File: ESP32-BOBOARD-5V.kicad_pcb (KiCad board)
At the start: 4 copper layers, 100 x 60 mm, 28 parts, among them J1 Conn_01x15, J2 Conn_01x15, J3 Conn_02x16_Counter_Clockwise, J4 Conn_01x03_Male, J5 DX07S016JA1R1500, U1 TXS0108EPW, U3 TXS0108EPW, U4 TXS0108EPW

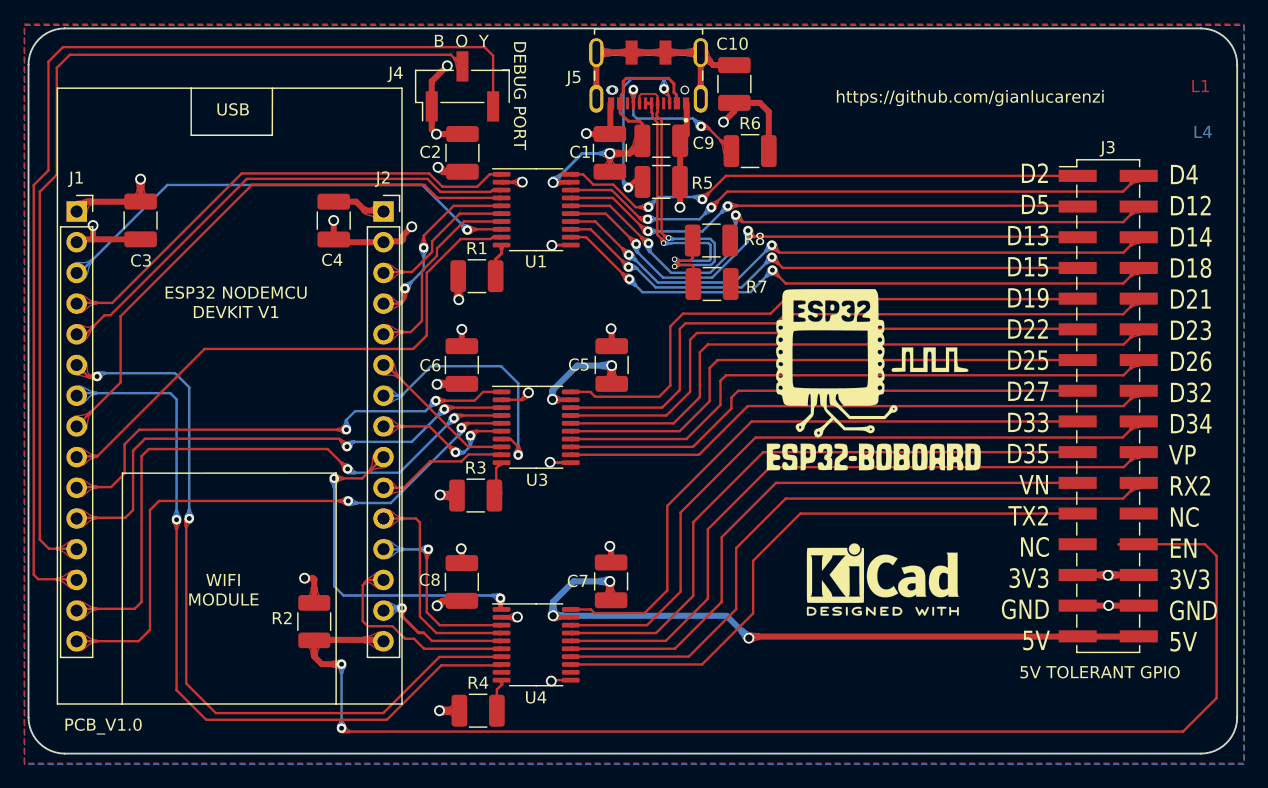
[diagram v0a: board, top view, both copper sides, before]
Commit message: Added the dip-switch for programming Added the ESP32 BOBOARD LOGO
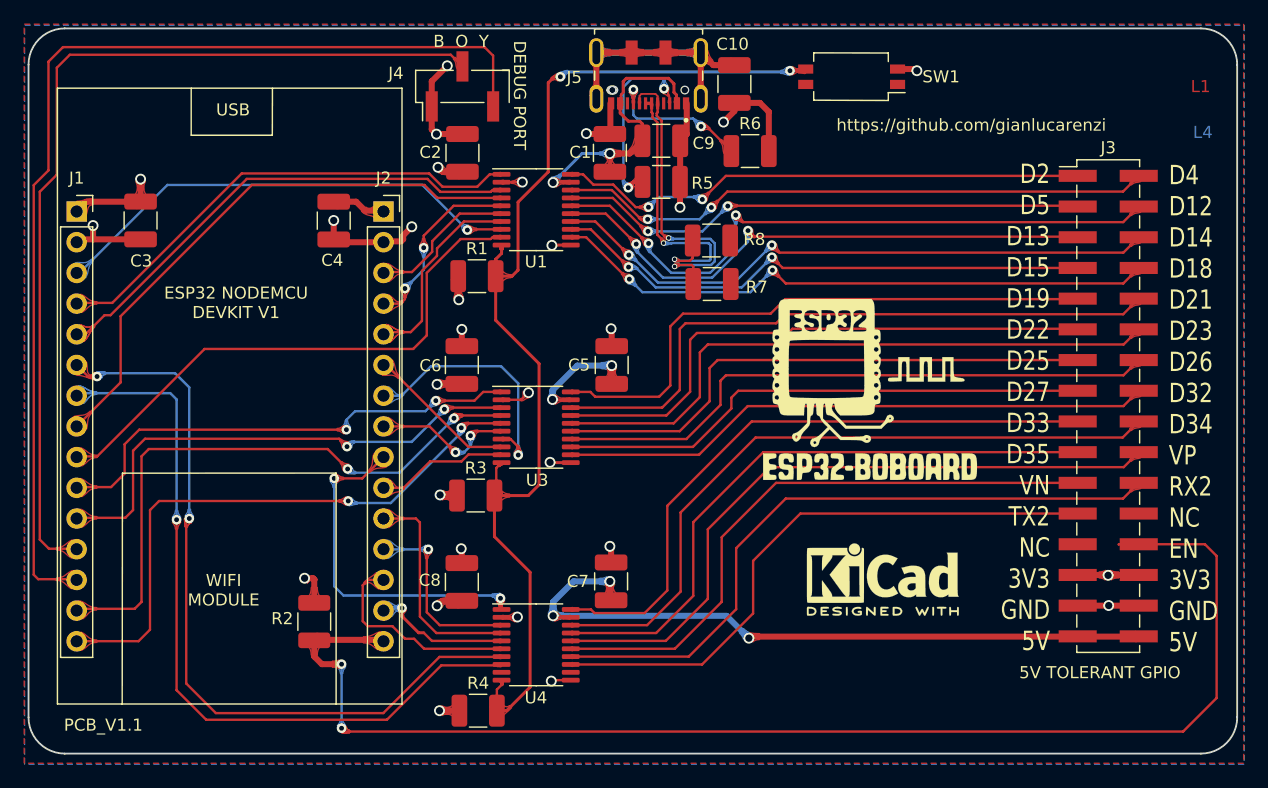
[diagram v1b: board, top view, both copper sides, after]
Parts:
- removed G***: LOGO, RetroBitLab:ESP32_BOBOARD_5V_21.7mmx21.7mm
- added GR2: LOGO, RetroBitLab:ESP32_BOBOARD_5V_21.7mmx21.7mm, F.Cu at (190.5, 104.5)
- added SW1: SPST_SWITCH_SMD_4P,4.1x5.4mm, RetroBitLab:SW_DIP_SPSTx02_DSHP02TS-S, F.Cu at (190.0, 78.0)
- renumbered L1 to GR1
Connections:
- R1 pad 2: Net-(R1-Pad2) -> TXS_EN
- R3 pad 2: Net-(R3-Pad2) -> TXS_EN
- R4 pad 2: Net-(R4-Pad2) -> TXS_EN
- U1 pad 10: Net-(R1-Pad2) -> TXS_EN
- U3 pad 10: Net-(R3-Pad2) -> TXS_EN
- U4 pad 10: Net-(R4-Pad2) -> TXS_EN
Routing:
- net TXS_EN: track 0.00 -> 92.2 mm, vias 0 -> 2
- net Net-(R3-Pad2): track 2.97 -> 0.00 mm
- net Net-(R1-Pad2): track 2.78 -> 0.00 mm
- net Net-(R4-Pad2): track 2.69 -> 0.00 mm
- net GND: track 74.9 -> 76.5 mm, vias 16 -> 17
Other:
- board text added: "PCB_V1.1"
- board text removed: "PCB_V1.0"

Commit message: Updated to reflect new components from library and LCSC availability
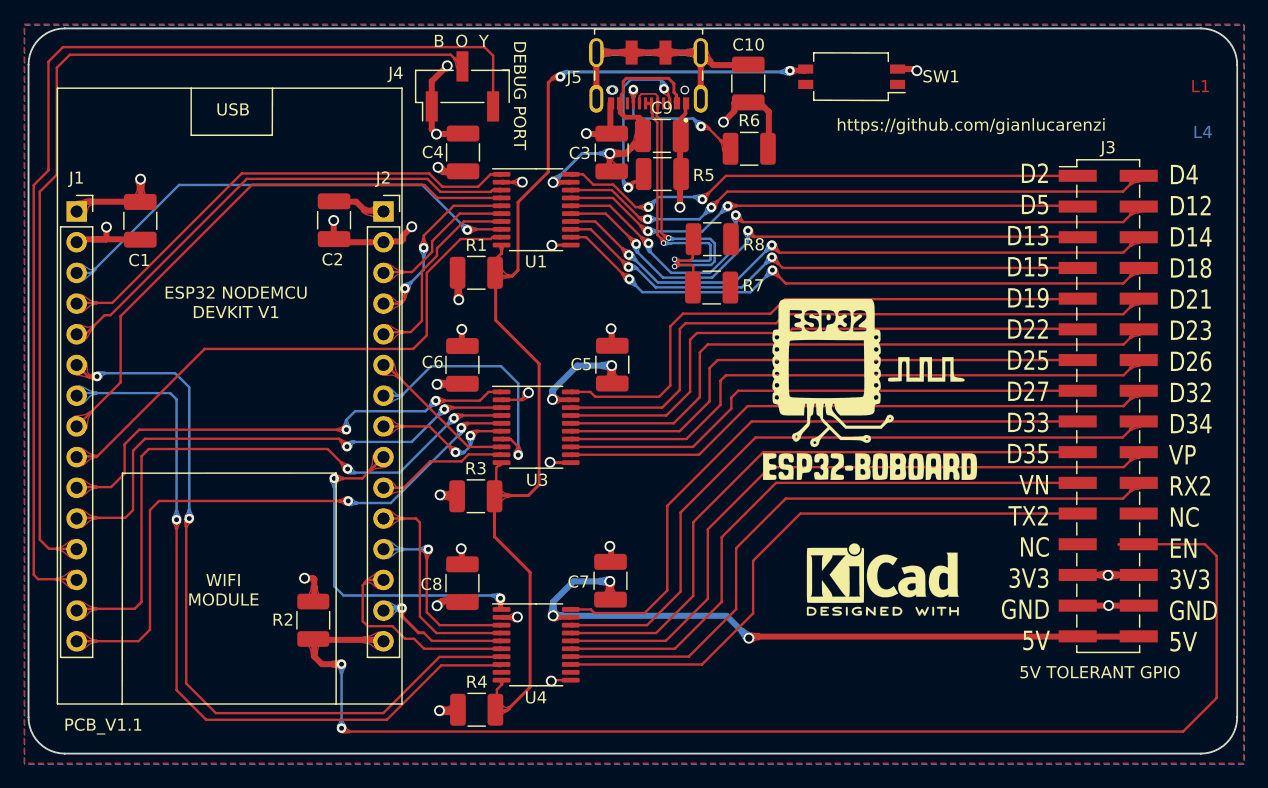
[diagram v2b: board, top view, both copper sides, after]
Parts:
- R5, R6: value 5.1K -> 5K1
- R7, R8: value 0R -> CREZ12101%
- moved C3 39.4 mm to (169.2, 84.3), turned to 90 degrees
- moved C1 39.3 mm to (130.2, 89.9), turned to 270 degrees
- moved C4 12.1 mm to (156.9, 84.3)
- moved C2 12.0 mm to (146.3, 89.9), turned to 270 degrees
- moved C10 1.15 mm to (180.6, 78.6), turned to 270 degrees
- moved R5 0.66 mm to (173.4, 86.0)
- moved C9 0.41 mm to (173.4, 82.9)
- moved R7 0.29 mm to (177.5, 95.4)
- moved R1 0.28 mm to (158.1, 94.2)
- moved R6 0.20 mm to (180.6, 84.0), turned to 180 degrees
- moved R4 0.14 mm to (158.1, 130.4)
- moved R2 0.14 mm to (144.6, 123.0), turned to 90 degrees
- moved R8 0.13 mm to (177.6, 91.4)
- moved C8 0.11 mm to (156.9, 119.9)
- moved C7 0.07 mm to (169.2, 119.7)
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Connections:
- C1 pad 1: +5V -> +3V3
- C10 pad 1: GND -> Net-(C10-Pad1)
- C10 pad 2: Net-(C10-Pad2) -> GND
- C2 pad 1: +3V3 -> +5V
- C3 pad 1: +3V3 -> +5V
- C4 pad 1: GND -> +3V3
- C4 pad 2: +5V -> GND
- J5 pad S1: Net-(C10-Pad2) -> Net-(C10-Pad1)
- J5 pad S2: Net-(C10-Pad2) -> Net-(C10-Pad1)
- J5 pad S3: Net-(C10-Pad2) -> Net-(C10-Pad1)
- J5 pad S4: Net-(C10-Pad2) -> Net-(C10-Pad1)
- J5 pad S5: Net-(C10-Pad2) -> Net-(C10-Pad1)
- J5 pad S6: Net-(C10-Pad2) -> Net-(C10-Pad1)
- R2 pad 1: +3V3 -> /EN
- R2 pad 2: /EN -> +3V3
- R6 pad 1: Net-(J5-Pad9) -> GND
- R6 pad 2: GND -> Net-(J5-Pad9)
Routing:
- net Net-(C10-Pad2): track 28.2 -> 0.00 mm
- net Net-(C10-Pad1): track 0.00 -> 28.2 mm
- net GND: track 76.5 -> 77.3 mm

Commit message: From 1210 to 0805 as the first are pretty hard to find nowadays.
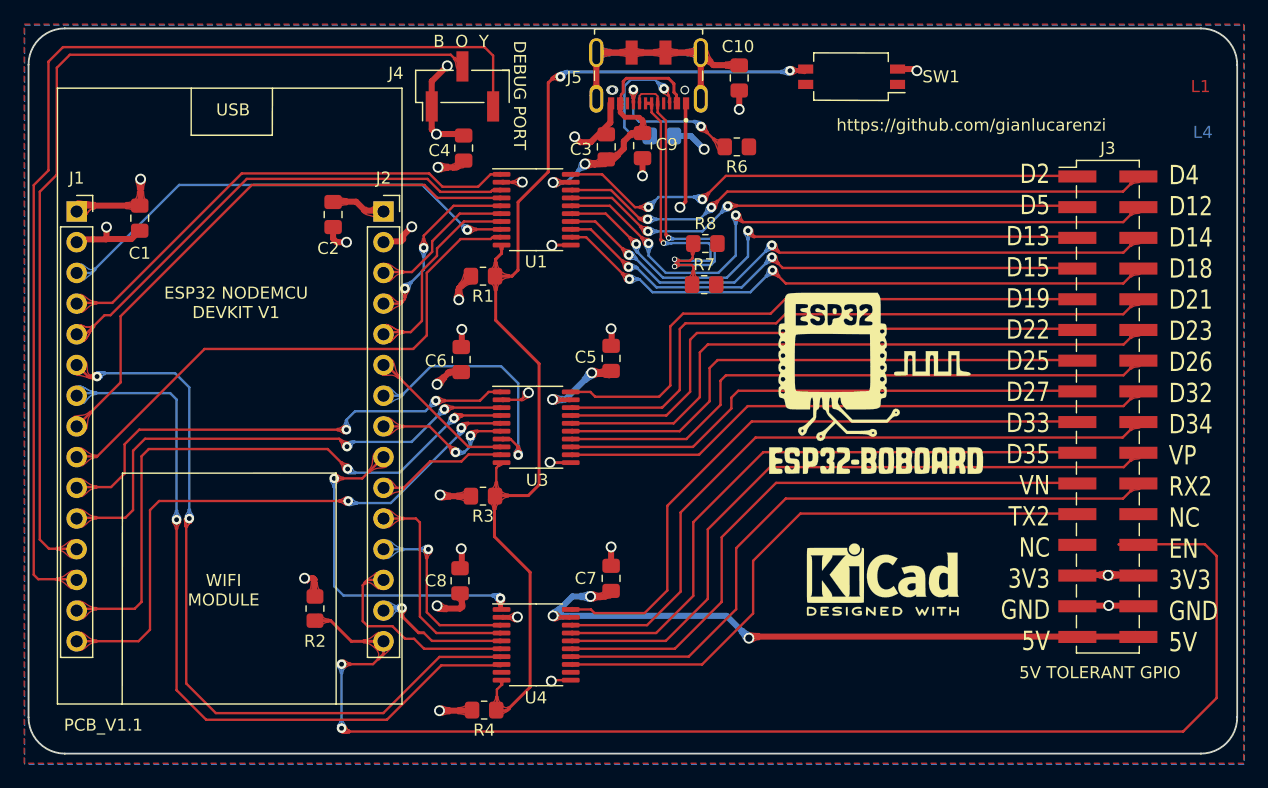
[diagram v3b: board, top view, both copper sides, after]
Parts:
- C1, C10, C2, C3, C4, C5, C6, C7, C8, C9: footprint Capacitor_SMD:C_1210_3225Metric_Pad1.33x2.70mm_HandSolder -> Capacitor_SMD:C_0805_2012Metric_Pad1.18x1.45mm_HandSolder
- J3: value Conn_02x16_Counter_Clockwise -> CONN_02x16_PIN_SMD_Counter_Clockwise
- R1, R2, R3, R4, R6: footprint Resistor_SMD:R_1210_3225Metric_Pad1.30x2.65mm_HandSolder -> Resistor_SMD:R_0805_2012Metric_Pad1.20x1.40mm_HandSolder
- R5: footprint Resistor_SMD:R_1210_3225Metric_Pad1.30x2.65mm_HandSolder -> Resistor_SMD:R_0805_2012Metric_Pad1.20x1.40mm_HandSolder; moved to B.Cu
- R7, R8: value CREZ12101% -> CREZ08051%; footprint Resistor_SMD:R_1210_3225Metric_Pad1.30x2.65mm_HandSolder -> Resistor_SMD:R_0805_2012Metric_Pad1.20x1.40mm_HandSolder
- moved R5 3.15 mm to (173.4, 82.9)
- moved C9 1.79 mm to (171.8, 83.7), turned to 270 degrees
- moved R6 1.04 mm to (179.6, 83.8)
- moved R2 0.98 mm to (144.7, 122.0)
- moved C10 0.88 mm to (179.8, 78.1)
- moved GR2 0.71 mm to (191.0, 104.0)
- moved R8 0.67 mm to (177.0, 91.8)
- moved R7 0.66 mm to (176.9, 95.2)
- moved C3 0.65 mm to (168.8, 83.8)
- moved R4 0.62 mm to (158.7, 130.4), turned to 180 degrees
- moved R1 0.62 mm to (158.6, 94.5), turned to 180 degrees
- moved R3 0.59 mm to (158.6, 112.7), turned to 180 degrees
- moved C5 0.53 mm to (169.2, 101.3)
- moved C2 0.48 mm to (146.2, 89.4)
- moved C6 0.45 mm to (156.8, 101.4)
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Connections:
- R1 pad 1: +3V3 -> TXS_EN
- R1 pad 2: TXS_EN -> +3V3
- R3 pad 1: +3V3 -> TXS_EN
- R3 pad 2: TXS_EN -> +3V3
- R4 pad 1: +3V3 -> TXS_EN
- R4 pad 2: TXS_EN -> +3V3
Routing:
- net +5V: track 149.9 -> 143.9 mm
- net GND: track 77.3 -> 72.4 mm, vias 17 -> 19
- net Net-(J5-Pad3): track 15.4 -> 11.0 mm, vias 2 -> 1
- net +3V3: track 31.9 -> 36.1 mm
- net /EN: track 108.9 -> 110.5 mm
- net /mD13: track 47.7 -> 48.4 mm
- net /mD12: track 53.9 -> 54.6 mm
- net Net-(J5-Pad9): track 12.6 -> 11.9 mm

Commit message: No BOTTOM components
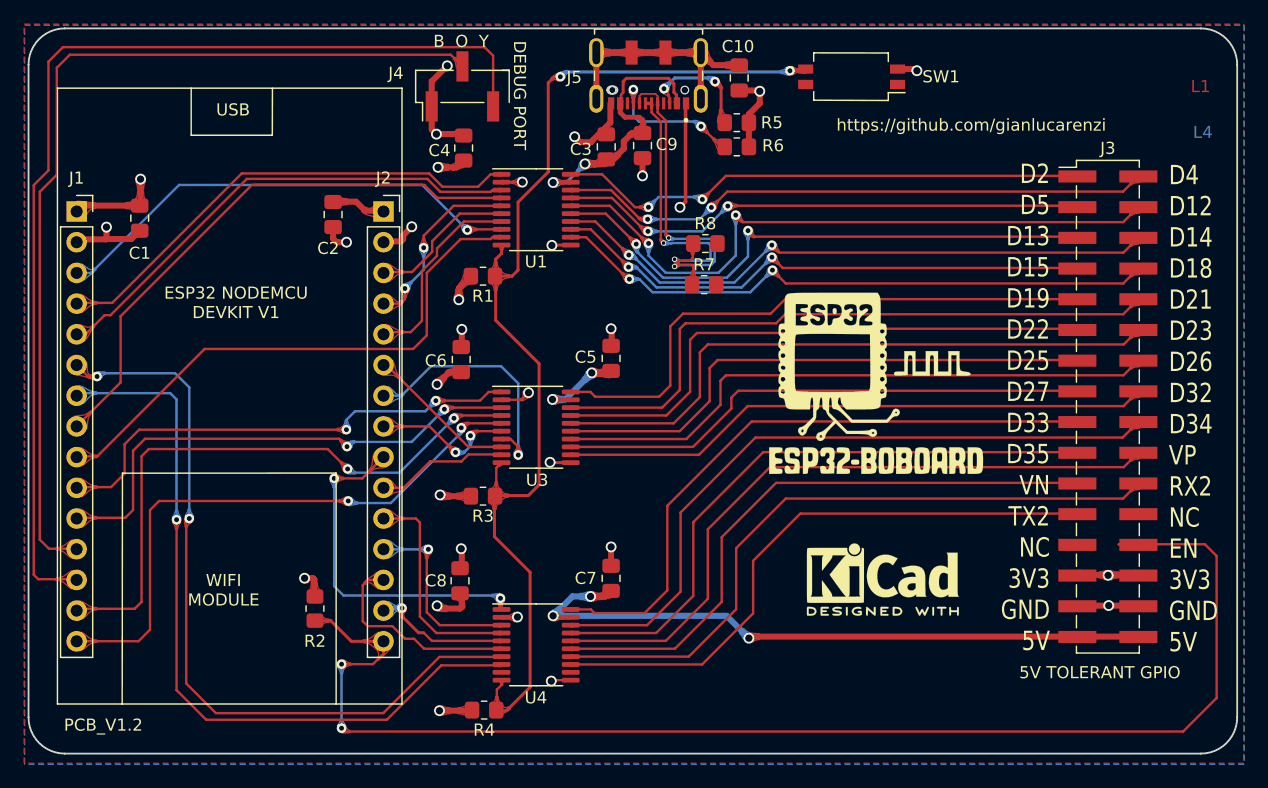
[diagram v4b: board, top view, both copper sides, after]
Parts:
- R5: moved to F.Cu
- moved R5 6.30 mm to (179.6, 81.8)
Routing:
- net GND: track 72.4 -> 74.6 mm, vias 19 -> 18
- net Net-(J5-Pad3): track 11.0 -> 9.84 mm, vias 1 -> 2
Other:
- board text added: "PCB_V1.2"
- board text removed: "PCB_V1.1"
